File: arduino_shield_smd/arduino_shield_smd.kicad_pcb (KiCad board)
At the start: 2 copper layers, 68.6 x 53.3 mm, 37 parts, among them J1 Power, J2 Digital/PWM, J3 Analog, J4 Digital/PWM, U1 ULN2803A, U2 ULN2803A, U3 PCF8574T, U4 PCF8574T

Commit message: second commit
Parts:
- added C1: 1uF, Capacitor_SMD:C_1206_3216Metric, F.Cu at (150.1, 124.3)
- added C2: 100nF, Capacitor_SMD:C_0603_1608Metric, F.Cu at (154.7, 124.7)
- added C3: 22uF, Capacitor_Tantalum_SMD:CP_EIA-3528-15_AVX-H, F.Cu at (135.1, 105.5)
- added C4: 1uF, Capacitor_SMD:C_1206_3216Metric, F.Cu at (139.2, 105.5)
- added C5: 1uF, Capacitor_SMD:C_1206_3216Metric, F.Cu at (144.6, 82.8)
- added C6: 1uF, Capacitor_SMD:C_1206_3216Metric, F.Cu at (144.6, 108.5)
- added D4: 2A, Diode_SMD:D_SMB, F.Cu at (130.3, 105.7)
- added RN1: 1K, Resistor_SMD:R_Array_Convex_4x0603, F.Cu at (138.5, 99.5)
- added RN2: 1K, Resistor_SMD:R_Array_Convex_4x0603, F.Cu at (134.1, 99.5)
- added RN3: 1K, Resistor_SMD:R_Array_Convex_4x0603, F.Cu at (138.5, 125.7)
- added RN4: 1K, Resistor_SMD:R_Array_Convex_4x0603, F.Cu at (134.1, 125.7)
- added TP1: GND, TestPoint:TestPoint_THTPad_3.0x3.0mm_Drill1.5mm, F.Cu at (156.4, 108.0)
- added TP2: +5V, TestPoint:TestPoint_THTPad_3.0x3.0mm_Drill1.5mm, F.Cu at (156.4, 101.0)
- added TP3: VIN, TestPoint:TestPoint_THTPad_3.0x3.0mm_Drill1.5mm, F.Cu at (156.4, 94.0)
- D1, D2, D3: footprint LED_SMD:LED_0603_1608Metric -> LED_SMD:LED_0805_2012Metric
- JA2: renamed from JP2A; footprint ayab-library:Molex_SPOX_5267-03A_1x03_P2.50mm_Vertical -> ayab-library:Molex_0022035035 or Hirose_HNC2-2.5P-3DS
- JA3: renamed from JP3A; footprint ayab-library:Molex_SPOX_5267-08A_1x08_P2.50mm_Vertical -> ayab-library:Molex_0022035085 or Hirose_HNC2_2.5P_8DS
- JA4: renamed from JP4A; footprint ayab-library:Molex_SPOX_5267-10A_1x10_P2.50mm_Vertical -> ayab-library:Molex_0022035105 or Hirose_HNC2-2.5P-10DS
- JA5: renamed from JP5; value 1X10 2.5mm -> HNC2-2.5P-10DS(55); footprint ayab-library:SHDR10W70P0X250_1X10_2740X490X590P -> ayab-library:HNC2-2.5P-10DS
- R1: renamed from R3; footprint Resistor_SMD:R_0603_1608Metric -> Resistor_SMD:R_0805_2012Metric
- R2: renamed from R5; value 150 -> 100; footprint Resistor_SMD:R_0603_1608Metric -> Resistor_SMD:R_0805_2012Metric
- R3: renamed from R4; value 150 -> 100; footprint Resistor_SMD:R_0603_1608Metric -> Resistor_SMD:R_0805_2012Metric
- R4: renamed from R2; value 5K -> 4.7K; footprint Resistor_SMD:R_0603_1608Metric -> Resistor_SMD:R_0805_2012Metric
- R5: renamed from R1; value 5K -> 4.7K; footprint Resistor_SMD:R_0603_1608Metric -> Resistor_SMD:R_0805_2012Metric
- U1: renamed from U4; footprint Package_SO:SOIC-18W_7.5x11.6mm_P1.27mm -> Package_SO:SOIC-16W_7.5x10.3mm_P1.27mm
- U2: footprint Package_SO:SOIC-16W_7.5x10.3mm_P1.27mm -> Package_SO:SOIC-18W_7.5x11.6mm_P1.27mm
- U3: footprint Package_SO:SOIC-18W_7.5x11.6mm_P1.27mm -> Package_SO:SOIC-16W_7.5x10.3mm_P1.27mm
- U4: renamed from U1; footprint Package_SO:SOIC-16W_7.5x10.3mm_P1.27mm -> Package_SO:SOIC-18W_7.5x11.6mm_P1.27mm
- moved REF** 51.8 mm to (169.9, 95.6)
- moved G*** 37.9 mm to (136.1, 126.7)
- moved R4 31.0 mm to (143.2, 103.8), turned to 180 degrees
- moved R5 26.9 mm to (143.2, 106.0), turned to 180 degrees
- moved JA2 22.0 mm to (174.9, 120.0), turned to 90 degrees
- moved JP9 19.9 mm to (158.0, 123.5), turned to 180 degrees
- moved JB3 13.5 mm to (119.4, 93.0)
- moved JB4 12.3 mm to (123.9, 127.2)
- moved U1 11.9 mm to (147.6, 90.4), turned to 90 degrees
- moved JB2 9.51 mm to (169.1, 121.1), turned to -90 degrees
- moved U4 8.98 mm to (134.5, 116.2)
- moved JB8 7.61 mm to (169.8, 87.6)
- moved JA7 6.49 mm to (175.9, 106.5)
- moved U3 6.27 mm to (147.6, 116.2), turned to 90 degrees
- moved JA8 6.08 mm to (175.5, 94.1)
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- renumbered JP7A to JA7, JP8A to JA8, JP2B to JB2, JP3B to JB3, JP4B to JB4, JP7B to JB7, JP8B to JB8
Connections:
- J1 pad 8: unconnected-(J1-Pin_8-Pad8) -> VIN
- JA3 pad 1: Net-(IC2-O1) -> Net-(JA3-Pin_1)
- JA3 pad 2: Net-(IC2-O2) -> Net-(JA3-Pin_2)
- JA4 pad 1: +15V -> VIN
- JA4 pad 2: +15V -> VIN
- JA4 pad 3: Net-(IC1-O1) -> Net-(JA4-Pin_3)
- JA4 pad 4: Net-(IC1-O2) -> Net-(JA4-Pin_4)
- JB3 pad 1: Net-(IC2-O1) -> Net-(JA3-Pin_1)
- JB3 pad 2: Net-(IC2-O2) -> Net-(JA3-Pin_2)
- JB4 pad 1: +15V -> VIN
- JB4 pad 2: +15V -> VIN
- JB4 pad 3: Net-(IC1-O1) -> Net-(JA4-Pin_3)
- JB4 pad 4: Net-(IC1-O2) -> Net-(JA4-Pin_4)
- R4 pad 1: (no net) -> /SCL
- R4 pad 2: (no net) -> +5V
- R5 pad 1: (no net) -> /SDA
- R5 pad 2: (no net) -> +5V
- REF** pad 1: (no net) -> GND
- REF** pad 10: (no net) -> GND
- REF** pad 11: (no net) -> GND
- REF** pad 12: (no net) -> GND
- REF** pad 13: (no net) -> GND
- REF** pad 14: (no net) -> GND
- REF** pad 15: (no net) -> GND
- REF** pad 16: (no net) -> GND
- REF** pad 17: (no net) -> GND
- REF** pad 18: (no net) -> GND
- REF** pad 19: (no net) -> GND
- REF** pad 2: (no net) -> GND
- REF** pad 20: (no net) -> GND
- REF** pad 21: (no net) -> GND
- REF** pad 22: (no net) -> GND
- REF** pad 23: (no net) -> GND
- REF** pad 24: (no net) -> GND
- REF** pad 25: (no net) -> GND
- REF** pad 26: (no net) -> GND
- REF** pad 27: (no net) -> GND
- REF** pad 28: (no net) -> GND
- REF** pad 29: (no net) -> GND
- REF** pad 3: (no net) -> GND
- REF** pad 30: (no net) -> GND
- REF** pad 31: (no net) -> GND
- REF** pad 32: (no net) -> GND
- REF** pad 33: (no net) -> GND
- REF** pad 34: (no net) -> GND
- REF** pad 35: (no net) -> GND
- REF** pad 36: (no net) -> GND
- REF** pad 37: (no net) -> GND
- REF** pad 38: (no net) -> GND
- REF** pad 39: (no net) -> GND
- REF** pad 4: (no net) -> GND
- REF** pad 40: (no net) -> GND
- REF** pad 41: (no net) -> GND
- REF** pad 42: (no net) -> GND
- REF** pad 43: (no net) -> GND
- REF** pad 44: (no net) -> GND
- REF** pad 45: (no net) -> GND
- REF** pad 46: (no net) -> GND
- REF** pad 47: (no net) -> GND
- REF** pad 48: (no net) -> GND
- REF** pad 49: (no net) -> GND
- REF** pad 5: (no net) -> GND
- REF** pad 50: (no net) -> GND
- REF** pad 51: (no net) -> GND
- REF** pad 52: (no net) -> GND
- REF** pad 53: (no net) -> GND
- REF** pad 54: (no net) -> GND
- REF** pad 55: (no net) -> GND
- REF** pad 56: (no net) -> GND
- REF** pad 57: (no net) -> GND
- REF** pad 58: (no net) -> GND
- REF** pad 59: (no net) -> GND
- REF** pad 6: (no net) -> GND
- REF** pad 60: (no net) -> GND
- REF** pad 61: (no net) -> GND
- REF** pad 62: (no net) -> GND
- REF** pad 63: (no net) -> GND
- REF** pad 64: (no net) -> GND
- REF** pad 65: (no net) -> GND
- REF** pad 66: (no net) -> GND
- REF** pad 67: (no net) -> GND
- REF** pad 68: (no net) -> GND
- REF** pad 69: (no net) -> GND
- REF** pad 7: (no net) -> GND
- REF** pad 70: (no net) -> GND
- REF** pad 71: (no net) -> GND
- REF** pad 72: (no net) -> GND
- REF** pad 73: (no net) -> GND
- REF** pad 74: (no net) -> GND
- REF** pad 75: (no net) -> GND
- REF** pad 76: (no net) -> GND
- REF** pad 77: (no net) -> GND
- REF** pad 78: (no net) -> GND
- REF** pad 79: (no net) -> GND
- REF** pad 8: (no net) -> GND
- REF** pad 80: (no net) -> GND
- REF** pad 81: (no net) -> GND
- REF** pad 82: (no net) -> GND
- REF** pad 83: (no net) -> GND
- REF** pad 9: (no net) -> GND
- U1 pad 1: /SCL -> +5V
- U1 pad 10: Net-(IC2-I1) -> Net-(RN2-R2.1)
- U1 pad 11: Net-(IC2-I2) -> Net-(RN2-R3.1)
- U1 pad 12: Net-(IC2-I3) -> Net-(RN2-R4.1)
- U1 pad 13: Net-(IC2-I4) -> unconnected-(U1-~{INT}-Pad13)
- U1 pad 14: Net-(IC2-I5) -> /SCL
- U1 pad 15: Net-(IC2-I6) -> /SDA
- U1 pad 16: Net-(IC2-I7) -> +5V
- U1 pad 2: /SDA -> GND
- U1 pad 4: GND -> Net-(RN1-R1.1)
- U1 pad 5: +5V -> Net-(RN1-R2.1)
- U1 pad 6: +5V -> Net-(RN1-R3.1)
- U1 pad 7: unconnected-(IC4-NC-Pad7) -> Net-(RN1-R4.1)
- U1 pad 8: unconnected-(IC4-INT-Pad8) -> GND
- U1 pad 9: GND -> Net-(RN2-R1.1)
- U2 pad 1: Net-(IC2-I1) -> Net-(RN1-R1.1)
- U2 pad 10: +15V -> VIN
- U2 pad 2: Net-(IC2-I2) -> Net-(RN1-R2.1)
- U2 pad 3: Net-(IC2-I3) -> Net-(RN1-R3.1)
- U2 pad 4: Net-(IC2-I4) -> Net-(RN1-R4.1)
- U2 pad 5: Net-(IC2-I5) -> Net-(RN2-R1.1)
- U2 pad 6: Net-(IC2-I6) -> Net-(RN2-R2.1)
- U2 pad 7: Net-(IC2-I7) -> Net-(RN2-R3.1)
- U2 pad 8: Net-(IC2-I8) -> Net-(RN2-R4.1)
- U3 pad 1: /SCL -> GND
- U3 pad 10: Net-(IC1-I1) -> Net-(RN4-R2.1)
- U3 pad 11: Net-(IC1-I2) -> Net-(RN4-R3.1)
- U3 pad 12: Net-(IC1-I3) -> Net-(RN4-R4.1)
- U3 pad 13: Net-(IC1-I4) -> unconnected-(U3-~{INT}-Pad13)
- U3 pad 14: Net-(IC1-I5) -> /SCL
- U3 pad 15: Net-(IC1-I6) -> /SDA
- U3 pad 16: Net-(IC1-I7) -> +5V
- U3 pad 2: /SDA -> GND
- U3 pad 4: GND -> Net-(RN3-R1.1)
- U3 pad 5: GND -> Net-(RN3-R2.1)
- U3 pad 6: +5V -> Net-(RN3-R3.1)
- U3 pad 7: unconnected-(IC3-NC-Pad7) -> Net-(RN3-R4.1)
- U3 pad 8: unconnected-(IC3-INT-Pad8) -> GND
- U3 pad 9: GND -> Net-(RN4-R1.1)
- U4 pad 1: Net-(IC1-I1) -> Net-(RN3-R1.1)
- U4 pad 10: +15V -> VIN
- U4 pad 2: Net-(IC1-I2) -> Net-(RN3-R2.1)
- U4 pad 3: Net-(IC1-I3) -> Net-(RN3-R3.1)
- U4 pad 4: Net-(IC1-I4) -> Net-(RN3-R4.1)
- U4 pad 5: Net-(IC1-I5) -> Net-(RN4-R1.1)
- U4 pad 6: Net-(IC1-I6) -> Net-(RN4-R2.1)
- U4 pad 7: Net-(IC1-I7) -> Net-(RN4-R3.1)
- U4 pad 8: Net-(IC1-I8) -> Net-(RN4-R4.1)
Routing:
- net +5V: track 21.0 -> 203.1 mm, vias 0 -> 4
- net VIN: track 0.00 -> 128.5 mm, vias 0 -> 1
- net /SCL: track 0.00 -> 94.9 mm, vias 0 -> 2
- net /SDA: track 140.3 -> 85.5 mm, vias 0 -> 2
- net /LED_GRN: track 0.00 -> 45.3 mm, vias 0 -> 1
- net /LED_YEL: track 0.00 -> 41.5 mm, vias 0 -> 1
- net Net-(RN2-R4.1): track 0.00 -> 26.7 mm
- net Net-(RN4-R4.1): track 0.00 -> 26.6 mm
- net Net-(RN2-R3.1): track 0.00 -> 26.5 mm
- net Net-(RN4-R3.1): track 0.00 -> 26.4 mm
- net Net-(RN4-R2.1): track 0.00 -> 26.3 mm
- net /ENC_B: track 13.3 -> 39.6 mm
- net Net-(RN2-R2.1): track 0.00 -> 26.2 mm
- net Net-(RN4-R1.1): track 0.00 -> 26.2 mm
- net Net-(RN2-R1.1): track 0.00 -> 25.9 mm
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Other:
- outline, holes or cut-outs redrawn
- board text added: "+5V"
- board text added: "+5V SDA SCL GND"
- board text added: "GND"
- board text added: "KI02.0"
- board text added: "VIN"
- board text removed: "GND SCL SDA +5V"

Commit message: OSHpark prototype
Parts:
- removed D4: 2A, Diode_SMD:D_SMB
- removed the G*** at (136.1, 126.7)
- removed the G*** at (148.4, 114.1)
- added G***: LOGO, LOGO, B.Cu at (140.8, 112.8)
- moved REF** 45.8 mm to (135.8, 126.2)
- moved C4 9.30 mm to (129.9, 105.3)
- moved REF** 6.11 mm to (139.7, 91.6)
- moved TP1 2.44 mm to (157.0, 110.4)
- moved TP2 2.44 mm to (157.0, 103.4)
- moved TP3 2.44 mm to (157.0, 96.4)
- moved C3 0.90 mm to (134.2, 105.5)
- renumbered JP9 to J5, JP6 to J6
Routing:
- net VIN: track 128.5 -> 127.4 mm
- net GND: vias 37 -> 54
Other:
- board text added: "AYAB Shield"
- board text added: "Woolly Logic"
- board text removed: "AYAB-Shield V1.6 4/2025"

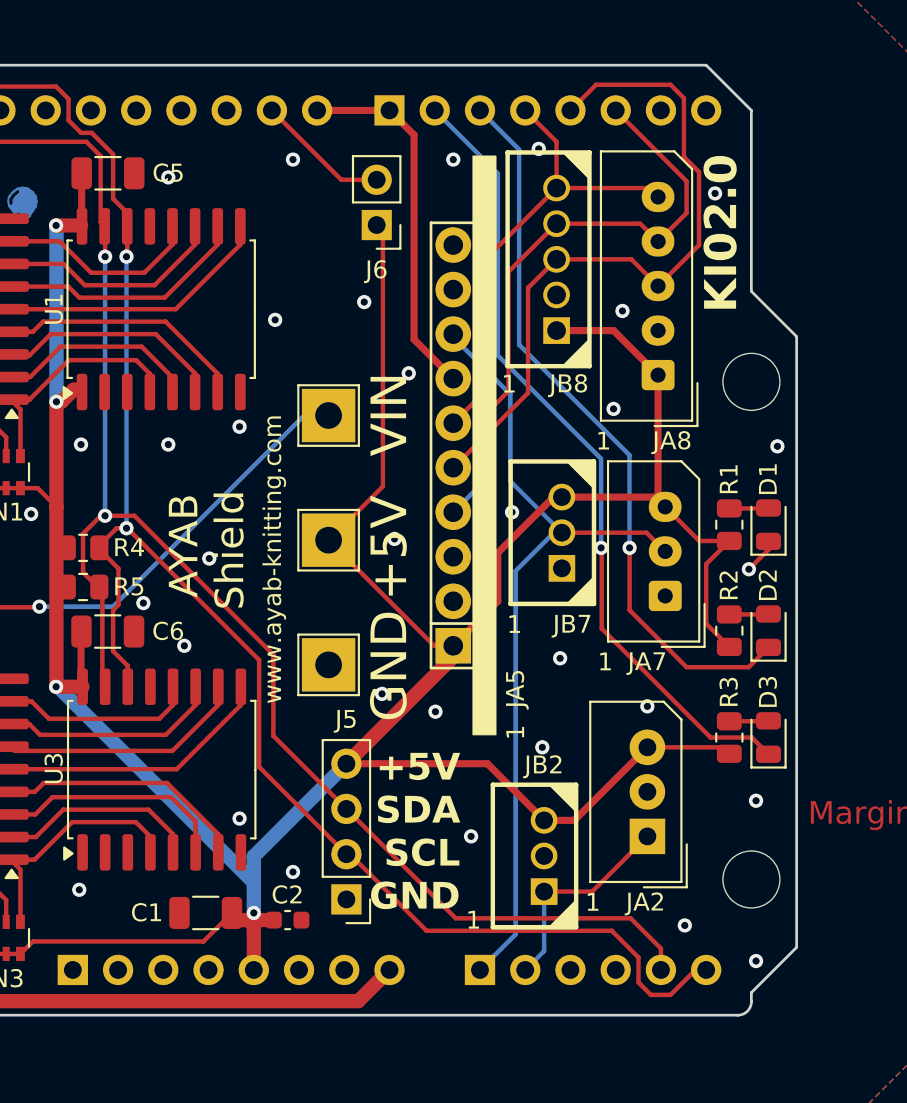
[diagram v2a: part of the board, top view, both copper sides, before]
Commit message: Add change LED footprints and add blue LED
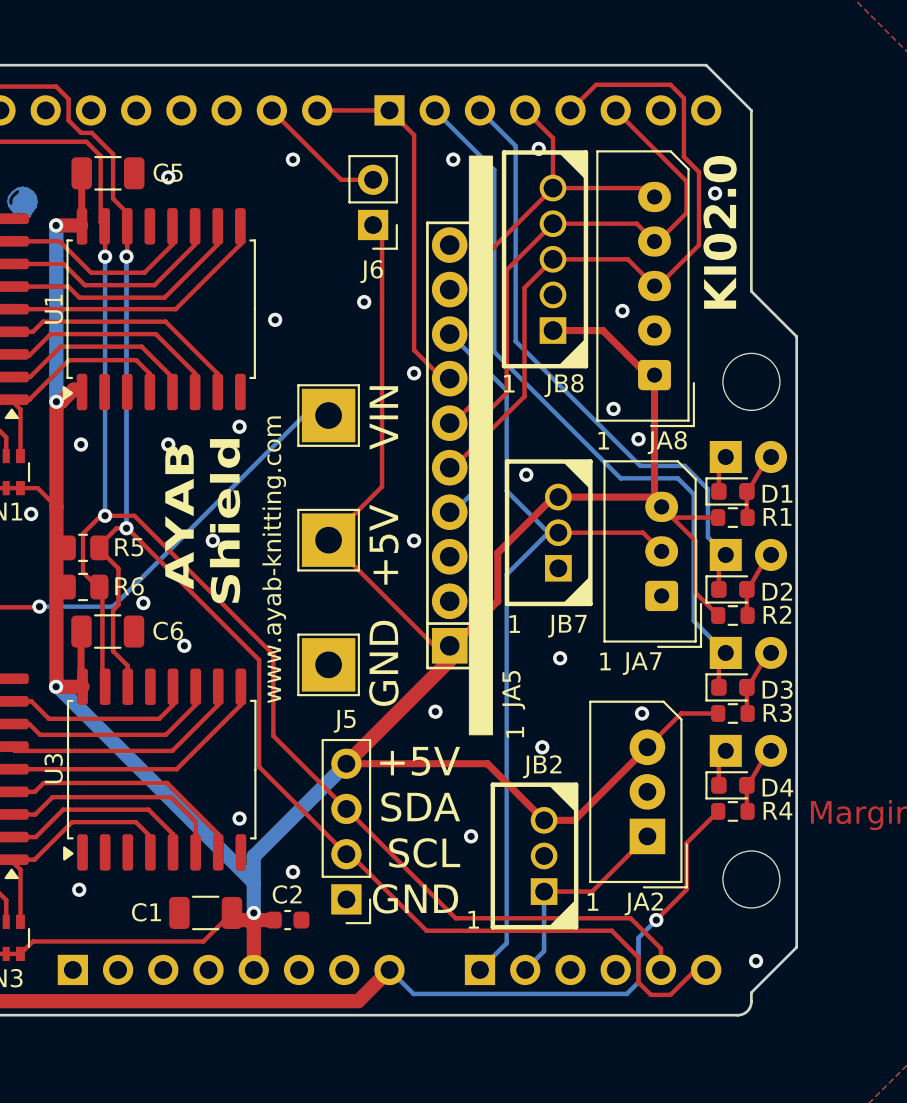
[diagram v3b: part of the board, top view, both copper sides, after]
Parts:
- added D4: BLUE_0603, ayab-library:LED_0603_3mm_THpads, F.Cu at (179.3, 115.2)
- added R4: 1K, ayab-library:R_0603_1608Metric, F.Cu at (179.7, 118.6)
- D1, D2, D3: footprint LED_SMD:LED_0805_2012Metric -> ayab-library:LED_0603_3mm_THpads
- R1, R3: footprint Resistor_SMD:R_0805_2012Metric -> ayab-library:R_0603_1608Metric
- R2: value 100 -> 150; footprint Resistor_SMD:R_0805_2012Metric -> ayab-library:R_0603_1608Metric
- moved D3 5.32 mm to (179.3, 109.7), turned to 0 degrees
- moved D2 4.88 mm to (179.3, 104.2), turned to 0 degrees
- moved D1 4.49 mm to (179.3, 98.7), turned to 0 degrees
- moved R3 1.36 mm to (179.7, 113.1), turned to 0 degrees
- moved R2 0.87 mm to (179.7, 107.6), turned to 0 degrees
- moved R1 0.45 mm to (179.7, 102.1), turned to 0 degrees
- moved JA7 0.20 mm to (175.7, 106.5)
- moved JB8 0.20 mm to (169.6, 87.6)
- moved J6 0.20 mm to (159.5, 85.7)
- moved JA5 0.20 mm to (163.8, 109.3)
- moved JA8 0.20 mm to (175.3, 94.1)
- moved JB7 0.20 mm to (169.9, 103.0)
- renumbered R4 to R5, R5 to R6
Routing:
- net VIN: track 127.4 -> 153.6 mm, vias 1 -> 2
- net /LED_YEL: track 41.5 -> 32.5 mm, vias 1 -> 0
- net /LED_GRN: track 45.3 -> 39.1 mm, vias 1 -> 0
- net GND: track 2.04 -> 0.02 mm, vias 54 -> 50
- net +5V: track 203.0 -> 201.4 mm
- net Net-(D4-A): track 0.00 -> 1.48 mm
- net Net-(D1-A): track 2.21 -> 1.48 mm
- net Net-(D3-A): track 2.21 -> 1.48 mm
- net Net-(D2-A): track 2.21 -> 1.48 mm

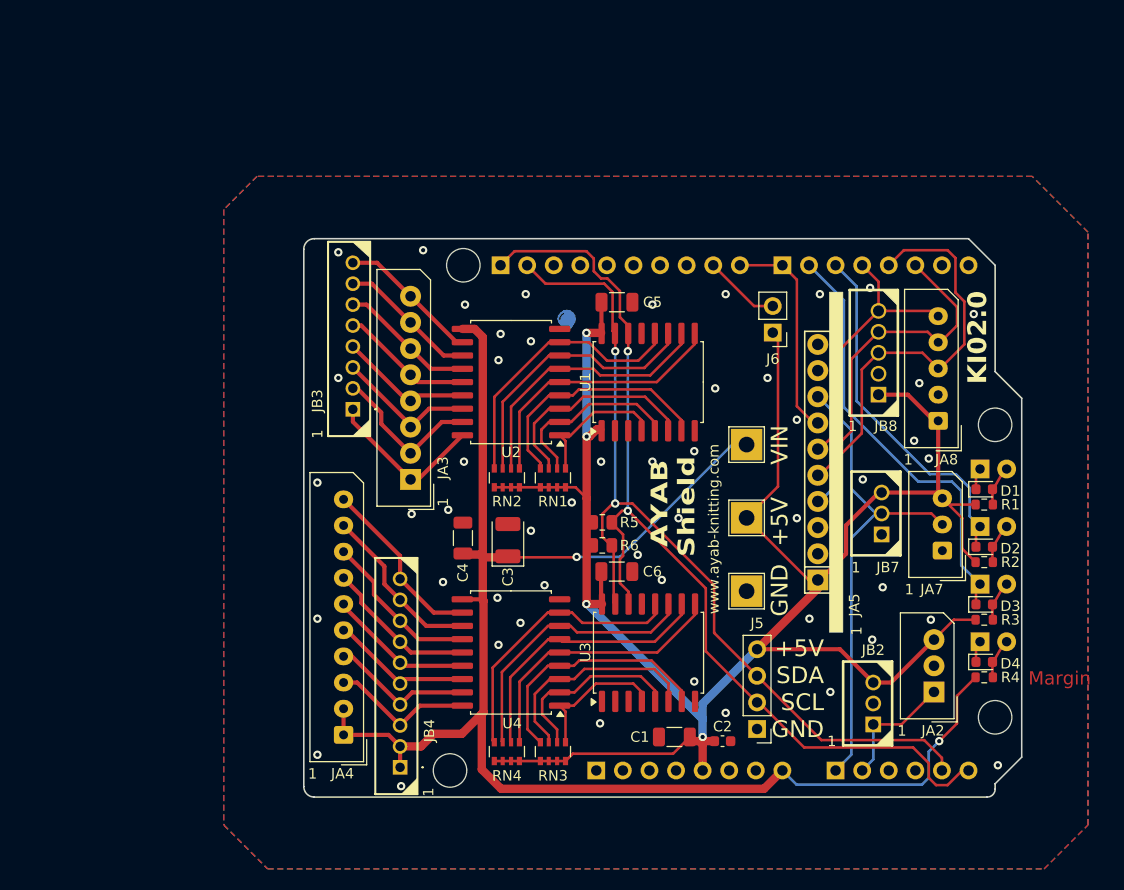
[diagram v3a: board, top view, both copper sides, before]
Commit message: Tweak top silkscreen
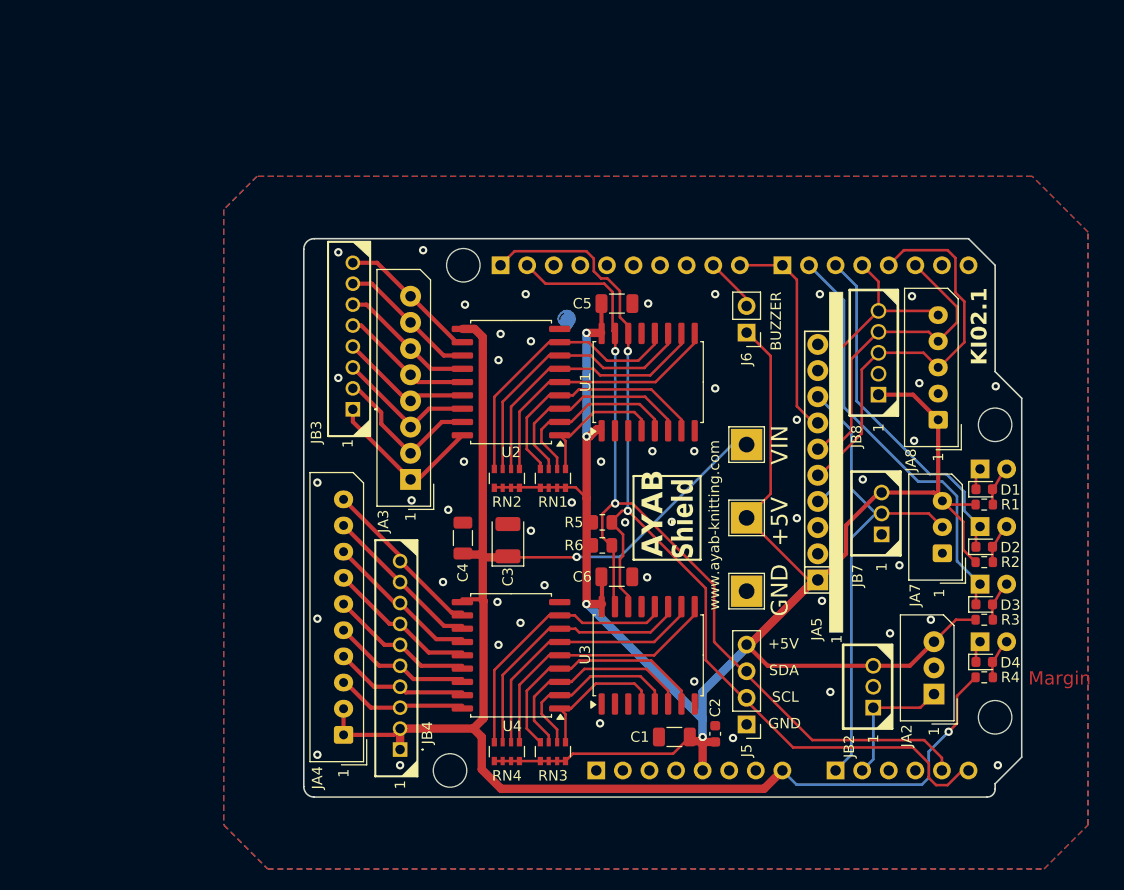
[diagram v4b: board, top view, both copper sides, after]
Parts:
- moved J6 2.50 mm to (157.0, 85.7)
- moved JB4 1.70 mm to (123.9, 125.5)
- moved JB2 1.60 mm to (169.1, 119.5)
- moved J5 1.09 mm to (157.0, 123.1)
- moved C2 0.99 mm to (154.0, 124.0), turned to 90 degrees
- moved C6 0.50 mm to (144.6, 109.0)
- moved U4 0.27 mm to (134.5, 116.5)
- moved U3 0.25 mm to (147.6, 116.5)
- moved JA7 0.25 mm to (175.7, 106.8)
- moved JA2 0.20 mm to (174.9, 120.2)
- moved C5 0.13 mm to (144.6, 82.9)
- moved JA8 0.10 mm to (175.3, 94.0)
- moved RN1 0.05 mm to (138.5, 99.6)
- moved RN2 0.05 mm to (134.1, 99.6)
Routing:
- net /BUZZ: track 7.30 -> 5.21 mm
- net VIN: track 153.6 -> 151.8 mm
- net Net-(JA4-Pin_3): track 13.8 -> 12.4 mm
- net Net-(RN1-R3.1): track 21.8 -> 20.7 mm
- net Net-(JA4-Pin_9): track 16.3 -> 15.3 mm
- net Net-(JA4-Pin_10): track 17.1 -> 16.1 mm
- net Net-(JA4-Pin_8): track 15.8 -> 14.8 mm
- net Net-(JA4-Pin_4): track 13.7 -> 12.8 mm
- net /EOL_L: track 11.9 -> 12.8 mm
- net Net-(RN4-R4.1): track 26.6 -> 26.0 mm
- net /LED_GRN: track 39.1 -> 38.6 mm
- net +5V: track 201.4 -> 202.0 mm
- net /LED_YEL: track 32.5 -> 32.0 mm
- net Net-(RN4-R3.1): track 26.4 -> 25.9 mm
- net /SDA: track 85.5 -> 86.0 mm
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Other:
- board text added: "AYAB"
- board text added: "BUZZER"
- board text added: "KI02.1"
- board text added: "SCL"
- board text added: "SDA"
- board text added: "Shield"
- board text removed: "+5V SDA SCL GND"
- board text removed: "AYAB Shield"
- board text removed: "KI02.0"

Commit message: Increase LED series resistor values to support Arduino Uno R4
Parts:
- R1, R2: value 150 -> 390
- R3: value 100 -> 220
- R4: value 1K -> 2K7
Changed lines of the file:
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@@
 			)
 		)
-		(property "Value" "1K"
+		(property "Value" "2K7"
 			(at 0 1.43 0)
 			(layer "F.Fab")
@@
 			)
 		)
-		(property "Mfg" "Broadcom"
+		(property "Mfg" ""
 			(at 0 0 0)
 			(unlocked yes)
@@
 			)
 		)
-		(property "Mfg P/N" "HLMP-1640-B00A1"
+		(property "Mfg P/N" ""
 			(at 0 0 0)
 			(unlocked yes)
@@
 			)
 		)
-		(property "Mfg" "Broadcom"
+		(property "Mfg" ""
 			(at 0 0 0)
 			(unlocked yes)
@@
 			)
 		)
-		(property "Mfg P/N" "HLMP-1640-B00A1"
+		(property "Mfg P/N" ""
 			(at 0 0 0)
 			(unlocked yes)
@@
 			)
 		)
-		(property "Mfg" "Broadcom"
+		(property "Mfg" ""
 			(at 0 0 0)
 			(unlocked yes)
@@
 			)
 		)
-		(property "Mfg P/N" "HLMP-1640-B00A1"
+		(property "Mfg P/N" ""
 			(at 0 0 0)
 			(unlocked yes)
@@
 			)
 		)
-		(property "Value" "100"
+		(property "Value" "220"
 			(at 0 1.43 0)
 			(layer "F.Fab")
@@
 			)
 		)
-		(property "Mfg" "Broadcom"
+		(property "Mfg" ""
 			(at 0 0 0)
 			(unlocked yes)
@@
 			)
 		)
-		(property "Mfg P/N" "HLMP-1640-B00A1"
+		(property "Mfg P/N" ""
 			(at 0 0 0)
 			(unlocked yes)
@@
 			)
 		)
-		(property "Value" "150"
+		(property "Value" "390"
 			(at 0 1.43 0)
 			(layer "F.Fab")
@@
 			)
 		)
-		(property "Value" "150"
+		(property "Value" "390"
 			(at 0 1.43 0)
 			(layer "F.Fab")
